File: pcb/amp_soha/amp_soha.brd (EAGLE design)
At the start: 100 x 80 mm, 55 parts, among them IC1 7812, IC2 7912, IC3 OPA2134PA, Q1 J113, Q2 J113, Q3 J113, Q4 J113, U1 TROCAR

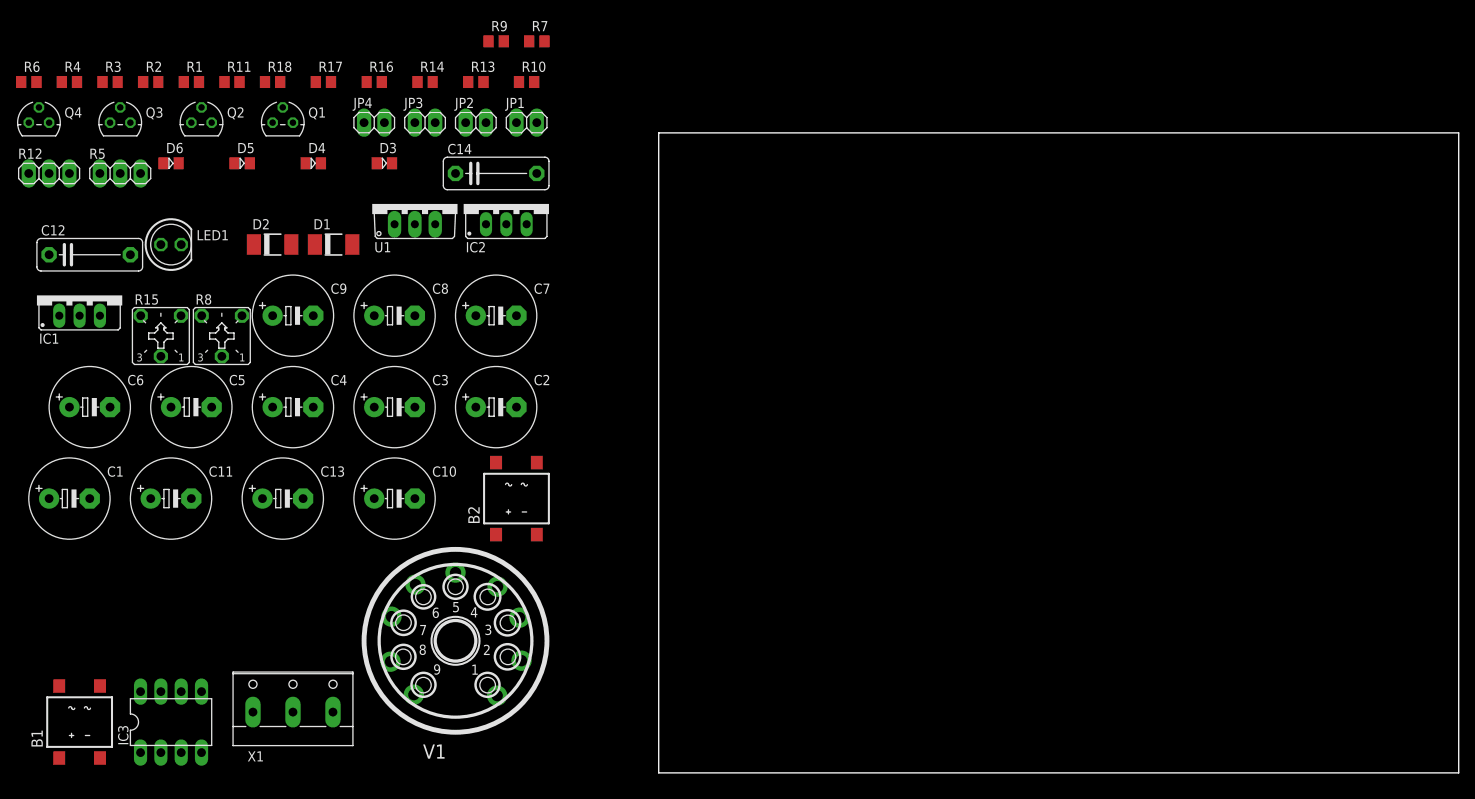
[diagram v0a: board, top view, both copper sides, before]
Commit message: 
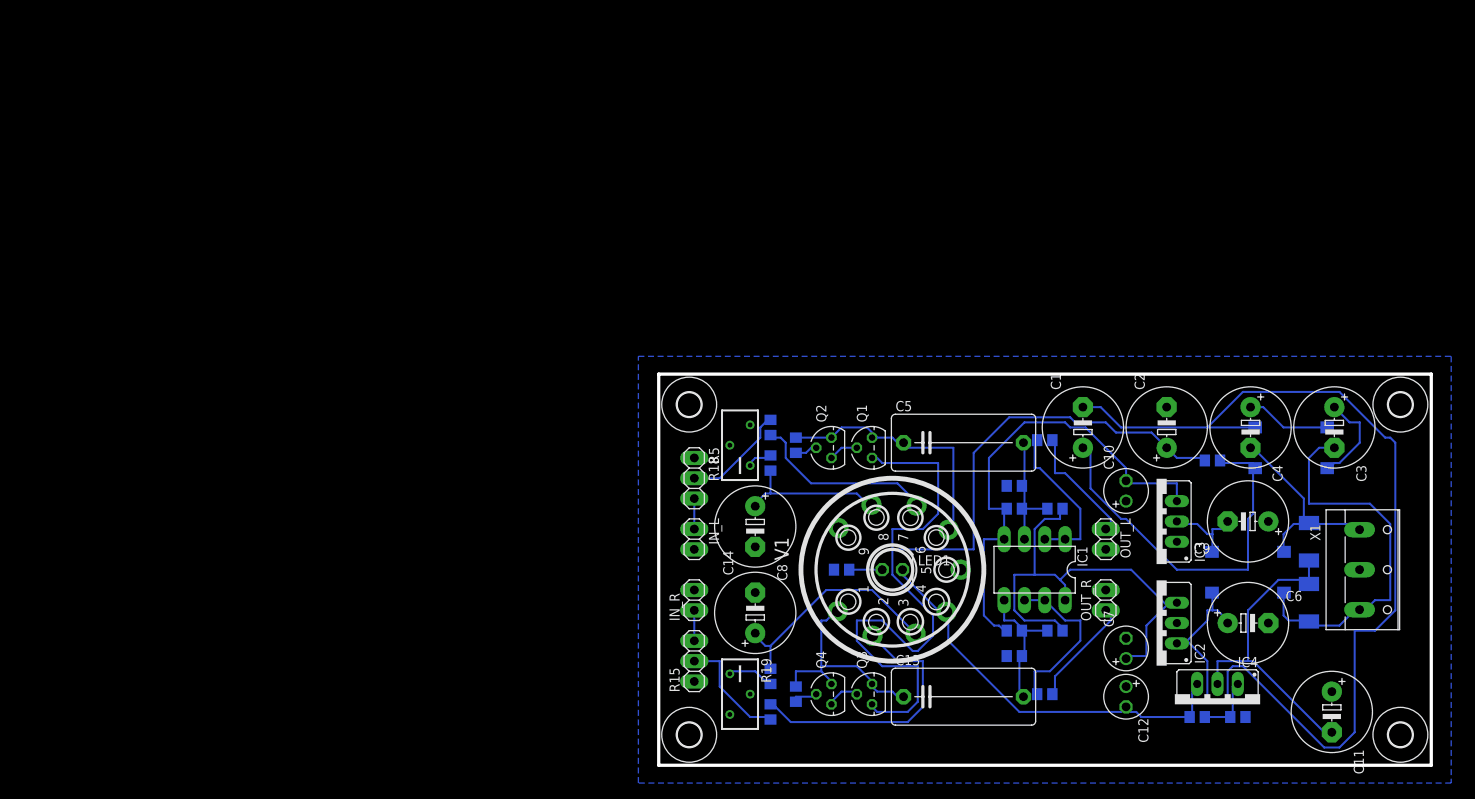
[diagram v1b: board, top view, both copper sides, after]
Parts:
- removed JP1, JP2, JP3, JP4: (no value), amp_soha:1X02
- removed R8: (no value), amp_soha:CT6
- removed U1: TROCAR, amp_soha:TO220AV
- added IC4: (no value), amp_soha:337TS
- added IN_L, IN_R, OUT_L, OUT_R: (no value), amp_soha:1X02
- added R19: (no value), amp_soha:RTRIM3296Y
- added U$1, U$2, U$3, U$4: (no value), amp_soha:3,0
- C1, C2, C3, C4: value (none) -> 100uF/100V
- C10, C7: value (none) -> 47uF/16V; device amp_soha:E5-10,5 -> amp_soha:E2,5-6
- C11, C6, C9: value (none) -> 470uF/35V
- C12: value (none) -> 47uF/16V; device amp_soha:C102-043X133 -> amp_soha:E2,5-6
- C13, C5: value (none) -> 1uF/100V; device amp_soha:E5-10,5 -> amp_soha:C150-072X183
- C14: value (none) -> 1000uF/10V; device amp_soha:C102-043X133 -> amp_soha:E5-10,5
- C8: value (none) -> 1000uF/10V
- D1, D2: value ES1 -> 1N4148; device amp_soha:DO-214AC -> amp_soha:D0805
- D3, D4: value 1N4148 -> ES1; device amp_soha:D0805 -> amp_soha:DO-214AC
- IC1: value 7812 -> OPA2134PA; device amp_soha:78XXS -> amp_soha:DIL08
- IC2: value 7912 -> 7812; device amp_soha:79XXS -> amp_soha:78XXS
- IC3: value OPA2134PA -> 7912; device amp_soha:DIL08 -> amp_soha:79XXS
- R1: value (none) -> 2k2
- R11: value (none) -> 11k
- R12: value (none) -> 360; device amp_soha:1X03 -> amp_soha:R0805
- R13, R3: value (none) -> 150
- R14, R4, R5: value (none) -> 100k
- R15: value (none) -> 100k; device amp_soha:CT6 -> amp_soha:1X03
- R16, R6: value (none) -> 300
- R17, R7: value (none) -> 560
- R18: device amp_soha:R0805 -> amp_soha:RTRIM3296Y
- R2: value (none) -> 360
- R9: value (none) -> 1k3
- moved B1 155.3 mm to (79.1, 40.6), flipped to the bottom, turned to 90 degrees
- moved R11 148.7 mm to (72.4, 6.99), flipped to the bottom
- moved C11 147.5 mm to (84.1, 7.62), turned to 270 degrees
- moved C6 147.3 mm to (73.7, 18.7)
- moved C12 140.8 mm to (58.4, 9.53), turned to 270 degrees
- moved R1 136.1 mm to (69.2, 39.1), flipped to the bottom, turned to 180 degrees
- moved X1 135.6 mm to (88.9, 25.4), turned to 270 degrees
- moved D4 133.1 mm to (81.3, 28.9), flipped to the bottom, turned to 270 degrees
- moved R4 128.4 mm to (44.5, 35.9), flipped to the bottom
- moved D3 128.0 mm to (81.3, 21.3), flipped to the bottom, turned to 90 degrees
- moved C1 127.0 mm to (53.0, 43.2), turned to 90 degrees
- moved IC3 125.7 mm to (62.2, 31.4), turned to 90 degrees
- moved R3 125.1 mm to (48.3, 41.6), flipped to the bottom, turned to 180 degrees
- moved IC1 124.2 mm to (47.0, 25.4), turned to 180 degrees
- moved Q4 122.1 mm to (21.6, 9.84), turned to 90 degrees
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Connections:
- removed net N$30: R14.2, R15.A
- net +12V: now also C7.+, D1.K, IC1.8, IC2.OUT; no longer C6.+, D3.K, IC1.OUT, IC3.8
- net +24V: now also C2.+, Q1.3, Q3.3, R1.1; no longer C10.+, Q2.3, Q4.3, R4.1
- net -12.6V: now also C12.-, IC4.3, R9.2; no longer C2.-, R1.2, U1.2
- net -12V: now also C10.-, D2.A, IC1.4, IC3.OUT; no longer C5.-, D4.A, IC2.OUT, IC3.4
- net AGND: now also C10.+, C11.+, C12.+, C14.-, C2.-, C7.-, C8.-, C9.+, IC3.GND, IN_L.2, IN_R.2, OUT_L.2, OUT_R.2, R10.1, R11.1, R14.2, R15.1, R18.2, R18.3, R19.2, R19.3, R4.2; no longer C1.+, C10.-, C11.-, C13.-, C2.+, C3.-, C4.+, C5.+, IC1.GND, JP1.2, JP2.2, JP3.2, JP4.2, R10.2, R12.1, R15.E, R15.S, R17.2, R2.1, R3.1, R8.E, R8.S
- net N$1: now also B2.AC1, C3.-, D3.C; no longer B1.AC1, C8.-, D1.C
- net N$10: now also R16.1, V1.2; no longer B2.-, C9.-
- net N$11: now also B1.+, C1.+, R1.2; no longer B2.+, C9.+, R4.2
- net N$12: now also IN_L.1; no longer JP1.1
- net N$14: now also V1.7; no longer V1.2
- net N$15: now also C8.+, V1.8; no longer C11.+, V1.3
- net N$16: now also Q2.2, R2.1; no longer Q1.2, R9.1
- net N$17: now also R18.1; no longer R8.A
- net N$18: now also R17.2, R19.1; no longer R13.1, V1.7
- net N$19: now also C5.1, R2.2, V1.6; no longer C12.1, R9.2, V1.1
- net N$2: now also B2.AC2, C4.-, D4.C; no longer B1.AC2, C7.-, D2.C
- net N$20: now also Q1.2, Q2.3; no longer Q1.3, Q2.2
- net N$22: now also C5.2, D1.A, D2.K, IC1.3, R4.1; no longer C12.2, D3.A, D4.K, IC3.3, R10.1
- net N$24: now also IC1.1, IC1.2, R3.1; no longer IC3.1, IC3.2, R11.1
- net N$25: now also OUT_L.1, R3.2; no longer JP2.1, R11.2
- net N$26: now also IN_R.1, R15.3; no longer JP3.1, R12.3
- net N$27: now also R15.2, R16.2; no longer R12.2, R13.2
- net N$29: now also C14.+, R17.1, V1.3; no longer C13.+, R14.1, V1.8
- net N$3: now also C11.-, D3.A, D4.A, IC4.2; no longer C1.-, D1.A, D2.A, U1.3
- net N$31: now also C13.1, R12.2, V1.1; no longer C14.1, R16.2, V1.6
- net N$32: now also Q4.2, R12.1; no longer Q3.2, R16.1
- net N$33: now also Q3.2, Q4.3; no longer Q3.3, Q4.2
- net N$34: now also C13.2, IC1.5, R14.1; no longer C14.2, IC3.5, R17.1
- net N$35: now also IC1.6, IC1.7, R13.1; no longer IC3.6, IC3.7, R18.1
- net N$36: now also OUT_R.1, R13.2; no longer JP4.1, R18.2
- net N$4: now also IC4.1, R11.2, R9.1; no longer R1.1, R2.2, U1.1
- net N$5: now also B2.-, C9.-, IC3.IN; no longer B1.-, C4.-, IC2.IN
- net N$6: now also B1.-, B2.+, C1.-, C6.+, IC2.IN; no longer B1.+, C3.+, IC1.IN
- net N$7: now also R10.2; no longer R3.2
- net N$8: now also B1.AC1, C3.+; no longer B2.AC1, C8.+
- net N$9: now also B1.AC2, C4.+; no longer B2.AC2, C7.+
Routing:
- net N$6: track 0.00 -> 139.1 mm
- net +24V: track 0.00 -> 126.6 mm
- net +12V: track 0.00 -> 60.5 mm
- net -12V: track 0.00 -> 59.9 mm
- net -12.6V: track 0.00 -> 51.4 mm
- net N$1: track 0.00 -> 48.8 mm
- net N$11: track 0.00 -> 48.5 mm
- net N$3: track 0.00 -> 39.3 mm
- net N$10: track 0.00 -> 34.4 mm
- net N$19: track 0.00 -> 32.8 mm
- net N$29: track 0.00 -> 28.9 mm
- net N$31: track 0.00 -> 28.5 mm
- net N$2: track 0.00 -> 25.6 mm
- net N$14: track 0.00 -> 23.6 mm
- net N$35: track 0.00 -> 20.9 mm
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- added copper zone on layer 16, net AGND
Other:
- board size 100 x 80 mm -> 96.6 x 48.9 mm

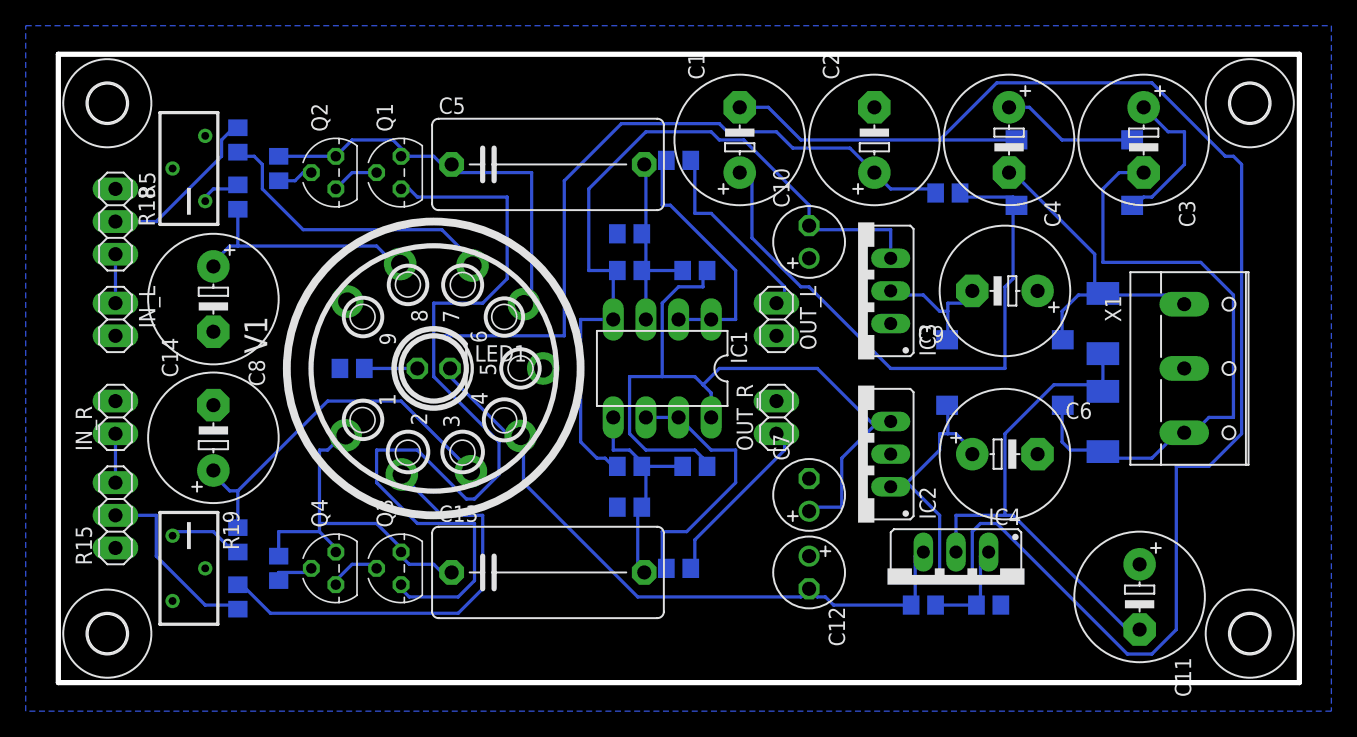
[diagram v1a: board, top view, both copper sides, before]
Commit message: 
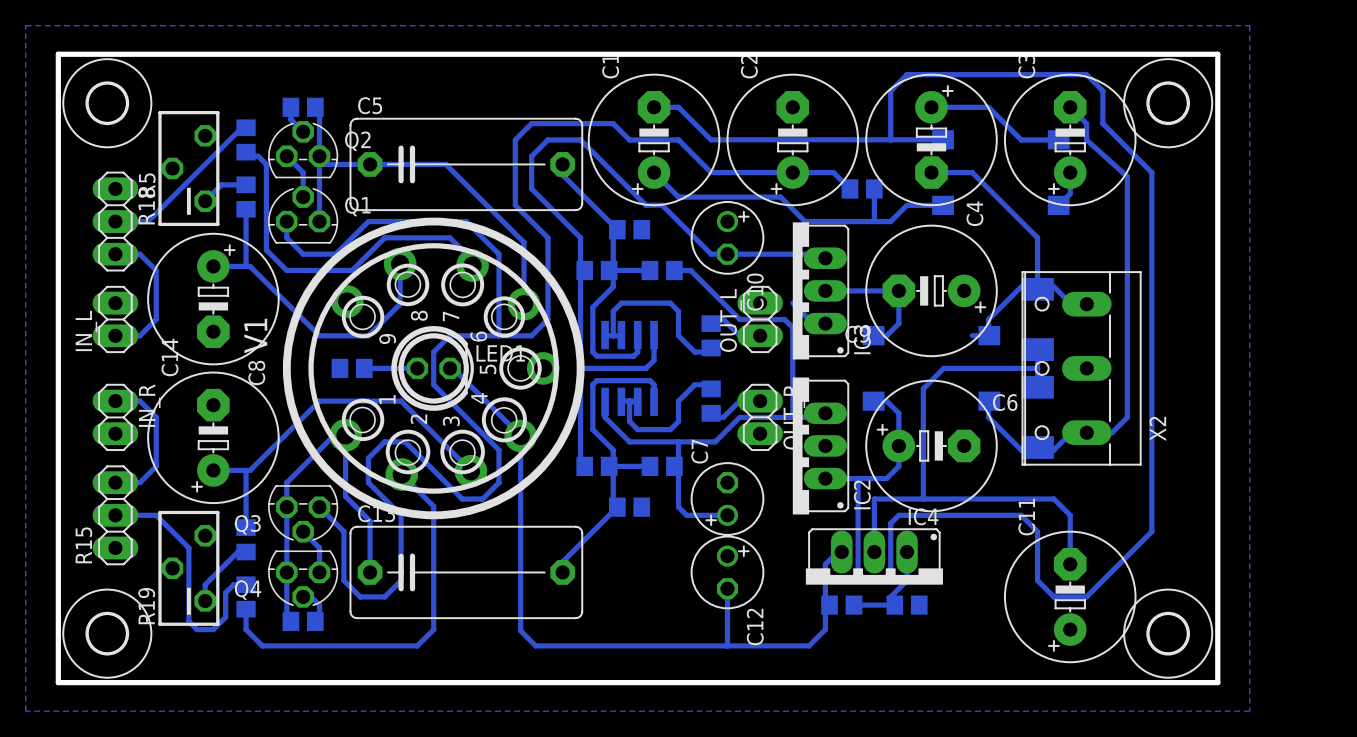
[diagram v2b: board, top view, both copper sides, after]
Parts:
- removed X1: (no value), amp_soha:W237-103
- added X2: (no value), amp_soha:W237-103
- IC1: value OPA2134PA -> NE5535U; device amp_soha:DIL08 -> amp_soha:SO08
- moved R3 13.9 mm to (50.8, 27.9), turned to 90 degrees
- moved R13 13.3 mm to (50.8, 22.9), turned to 270 degrees
- moved Q3 8.99 mm to (19.1, 14.6), turned to 180 degrees
- moved Q1 8.52 mm to (19.1, 36.8), turned to 0 degrees
- moved R1 6.68 mm to (62.5, 39.4)
- moved C1 6.67 mm to (46.4, 43.2)
- moved C10 6.36 mm to (52.1, 35.6), turned to 270 degrees
- moved C7 6.36 mm to (52.1, 15.2)
- moved C12 6.35 mm to (52.1, 9.53)
- moved C13 6.35 mm to (31.8, 9.53)
- moved C2 6.35 mm to (57.1, 43.2)
- moved C5 6.35 mm to (31.8, 41.3)
- moved R9 6.35 mm to (61.0, 6.99)
- moved IC4 6.35 mm to (63.5, 8.57)
- moved R11 6.35 mm to (66.0, 6.99)
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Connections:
- net AGND: now also X2.2; no longer X1.2
- net N$1: now also X2.1; no longer X1.3
- net N$2: now also X2.3; no longer X1.1
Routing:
- net N$11: track 48.5 -> 27.1 mm
- net +12V: track 60.5 -> 48.3 mm
- net N$22: track 15.6 -> 27.3 mm
- net N$25: track 15.5 -> 4.47 mm
- net N$36: track 14.1 -> 4.79 mm
- net N$8: track 11.9 -> 2.92 mm
- net N$34: track 18.2 -> 27.0 mm
- net N$1: track 48.8 -> 40.5 mm
- net -12.6V: track 51.4 -> 59.0 mm
- net N$12: track 3.81 -> 11.2 mm
- net N$26: track 3.81 -> 11.2 mm
- net N$35: track 20.9 -> 14.0 mm
- net N$15: track 18.8 -> 25.4 mm
- net N$24: track 19.7 -> 14.1 mm
- net N$3: track 39.3 -> 44.8 mm
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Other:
- board size 96.6 x 48.9 mm -> 90.2 x 48.9 mm
